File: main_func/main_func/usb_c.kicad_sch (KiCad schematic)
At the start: 6 parts, among them J1 USB_C_Receptacle_USB2.0, J2 Conn_01x05_Male

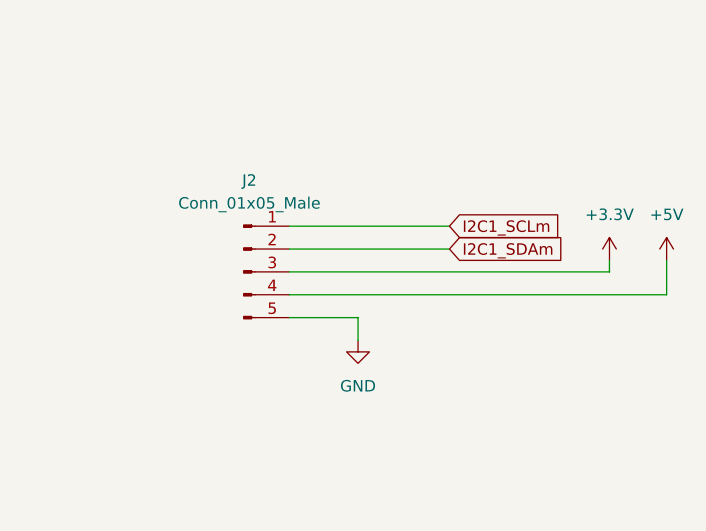
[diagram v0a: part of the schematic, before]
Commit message: main func schematics fixed
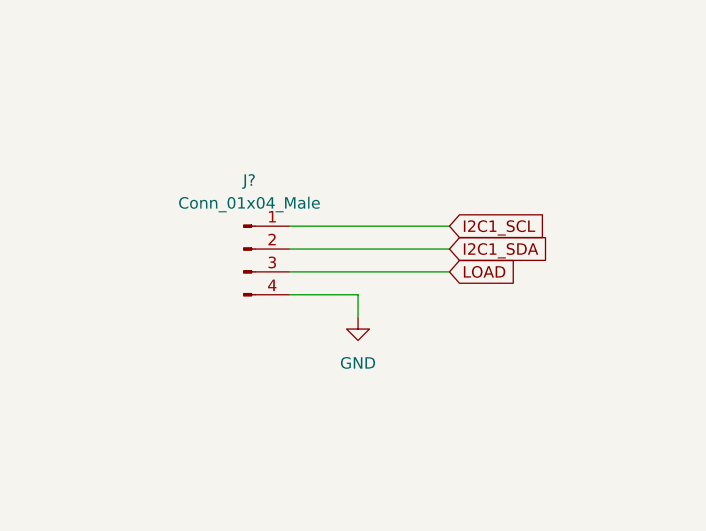
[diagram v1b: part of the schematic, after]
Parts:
- removed J2: Conn_01x05_Male, symbol Connector:Conn_01x05_Male
- added J?: Conn_01x04_Male, symbol Connector:Conn_01x04_Male
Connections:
- net GND: now also J?.4 (Pin_4)
- new net I2C1_SCL: J?.1 (Pin_1)
- new net I2C1_SDA: J?.2 (Pin_2)
- new net LOAD: J?.3 (Pin_3)
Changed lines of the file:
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@@
-    (stroke (width 0) (type default) (color 0 0 0 0))
-  )
-  (wire (pts (xy 163.83 69.85) (xy 205.74 69.85))
     (stroke (width 0) (type default) (color 0 0 0 0))
   )
@@
     (stroke (width 0) (type default) (color 0 0 0 0))
   )
-  (wire (pts (xy 171.45 72.39) (xy 171.45 74.93))
+  (wire (pts (xy 171.45 69.85) (xy 171.45 72.39))
     (stroke (width 0) (type default) (color 0 0 0 0))
   )
@@
     (stroke (width 0) (type default) (color 0 0 0 0))
   )
-  (wire (pts (xy 163.83 72.39) (xy 171.45 72.39))
+  (wire (pts (xy 163.83 69.85) (xy 171.45 69.85))
+    (stroke (width 0) (type default) (color 0 0 0 0))
+  )
+  (wire (pts (xy 163.83 67.31) (xy 181.61 67.31))
     (stroke (width 0) (type default) (color 0 0 0 0))
   )
@@
     (stroke (width 0) (type default) (color 0 0 0 0))
   )
-  (wire (pts (xy 205.74 69.85) (xy 205.74 66.04))
-    (stroke (width 0) (type default) (color 0 0 0 0))
-  )
-  (wire (pts (xy 163.83 67.31) (xy 199.39 67.31))
-    (stroke (width 0) (type default) (color 0 0 0 0))
-  )
   (wire (pts (xy 68.58 44.45) (xy 81.28 44.45))
     (stroke (width 0) (type default) (color 0 0 0 0))
@@
     (stroke (width 0) (type default) (color 0 0 0 0))
   )
-  (wire (pts (xy 199.39 67.31) (xy 199.39 66.04))
-    (stroke (width 0) (type default) (color 0 0 0 0))
-  )
   (wire (pts (xy 68.58 62.23) (xy 73.66 62.23))
     (stroke (width 0) (type default) (color 0 0 0 0))
@@
     )
   )
-  (global_label "I2C1_SDAm" (shape input) (at 181.61 64.77 0) (fields_autoplaced)
-    (effects (font (size 1.27 1.27)) (justify left))
-    (property "Intersheet References" "${INTERSHEET_REFS}" (id 0) (at 194.546 64.6906 0)
+  (global_label "I2C1_SDA" (shape input) (at 181.61 64.77 0) (fields_autoplaced)
+    (effects (font (size 1.27 1.27)) (justify left))
+    (property "Intersheet References" "${INTERSHEET_REFS}" (id 0) (at 192.8526 64.6906 0)
       (effects (font (size 1.27 1.27)) (justify left) hide)
     )
@@
     )
   )
-  (global_label "I2C1_SCLm" (shape input) (at 181.61 62.23 0) (fields_autoplaced)
-    (effects (font (size 1.27 1.27)) (justify left))
-    (property "Intersheet References" "${INTERSHEET_REFS}" (id 0) (at 194.4855 62.1506 0)
-      (effects (font (size 1.27 1.27)) (justify left) hide)
-    )
-  )
-  (symbol (lib_id "power:+5V") (at 205.74 66.04 0) (unit 1)
-    (in_bom yes) (on_board yes) (fields_autoplaced)
-    (property "Reference" "#PWR032" (id 0) (at 205.74 69.85 0)
-      (effects (font (size 1.27 1.27)) hide)
-    )
-    (property "Value" "+5V" (id 1) (at 205.74 60.96 0))
-    (property "Footprint" "" (id 2) (at 205.74 66.04 0)
-      (effects (font (size 1.27 1.27)) hide)
-    )
-    (property "Datasheet" "" (id 3) (at 205.74 66.04 0)
-      (effects (font (size 1.27 1.27)) hide)
-    )
-    (pin "1")
+  (global_label "I2C1_SCL" (shape input) (at 181.61 62.23 0) (fields_autoplaced)
+    (effects (font (size 1.27 1.27)) (justify left))
+    (property "Intersheet References" "${INTERSHEET_REFS}" (id 0) (at 192.7921 62.1506 0)
+      (effects (font (size 1.27 1.27)) (justify left) hide)
+    )
+  )
+  (global_label "LOAD" (shape input) (at 181.61 67.31 0) (fields_autoplaced)
+    (effects (font (size 1.27 1.27)) (justify left))
+    (property "Intersheet References" "${INTERSHEET_REFS}" (id 0) (at 188.7402 67.2306 0)
+      (effects (font (size 1.27 1.27)) (justify left) hide)
+    )
   )
   (symbol (lib_id "Device:R") (at 110.49 58.42 0) (unit 1)
@@
     (pin "2")
   )
-  (symbol (lib_id "power:+3.3V") (at 199.39 66.04 0) (unit 1)
-    (in_bom yes) (on_board yes) (fields_autoplaced)
-    (property "Reference" "#PWR031" (id 0) (at 199.39 69.85 0)
-      (effects (font (size 1.27 1.27)) hide)
-    )
-    (property "Value" "+3.3V" (id 1) (at 199.39 60.96 0))
-    (property "Footprint" "" (id 2) (at 199.39 66.04 0)
-      (effects (font (size 1.27 1.27)) hide)
-    )
-    (property "Datasheet" "" (id 3) (at 199.39 66.04 0)
-      (effects (font (size 1.27 1.27)) hide)
-    )
-    (pin "1")
-  )
   (symbol (lib_id "Device:R") (at 99.06 58.42 0) (unit 1)
     (in_bom yes) (on_board yes) (fields_autoplaced)
@@
     (pin "1")
     (pin "2")
-  )
-  (symbol (lib_id "Connector:Conn_01x05_Male") (at 158.75 67.31 0) (unit 1)
-    (in_bom yes) (on_board yes) (fields_autoplaced)
-    (property "Reference" "J2" (id 0) (at 159.385 57.15 0))
-    (property "Value" "Conn_01x05_Male" (id 1) (at 159.385 59.69 0))
-    (property "Footprint" "" (id 2) (at 158.75 67.31 0)
-      (effects (font (size 1.27 1.27)) hide)
-    )
-    (property "Datasheet" "~" (id 3) (at 158.75 67.31 0)
-      (effects (font (size 1.27 1.27)) hide)
-    )
-    (pin "1")
-    (pin "2")
-    (pin "3")
-    (pin "4")
-    (pin "5")
   )
   (symbol (lib_id "Connector:USB_C_Receptacle_USB2.0") (at 53.34 59.69 0) (unit 1)
@@
     (pin "S1")
   )
+  (symbol (lib_id "Connector:Conn_01x04_Male") (at 158.75 64.77 0) (unit 1)
+    (in_bom yes) (on_board yes) (fields_autoplaced)
+    (property "Reference" "J?" (id 0) (at 159.385 57.15 0))
+    (property "Value" "Conn_01x04_Male" (id 1) (at 159.385 59.69 0))
+    (property "Footprint" "" (id 2) (at 158.75 64.77 0)
+      (effects (font (size 1.27 1.27)) hide)
+    )
+    (property "Datasheet" "~" (id 3) (at 158.75 64.77 0)
+      (effects (font (size 1.27 1.27)) hide)
+    )
+    (pin "1")
+    (pin "2")
+    (pin "3")
+    (pin "4")
+  )
   (symbol (lib_id "Device:Polyfuse") (at 85.09 44.45 90) (unit 1)
     (in_bom yes) (on_board yes) (fields_autoplaced)
@@
     (pin "1")
   )
-  (symbol (lib_id "power:GND") (at 171.45 74.93 0) (unit 1)
-    (in_bom yes) (on_board yes) (fields_autoplaced)
-    (property "Reference" "#PWR030" (id 0) (at 171.45 81.28 0)
-      (effects (font (size 1.27 1.27)) hide)
-    )
-    (property "Value" "GND" (id 1) (at 171.45 80.01 0))
-    (property "Footprint" "" (id 2) (at 171.45 74.93 0)
-      (effects (font (size 1.27 1.27)) hide)
-    )
-    (property "Datasheet" "" (id 3) (at 171.45 74.93 0)
-      (effects (font (size 1.27 1.27)) hide)
-    )
+  (symbol (lib_id "power:GND") (at 171.45 72.39 0) (unit 1)
+    (in_bom yes) (on_board yes) (fields_autoplaced)
+    (property "Reference" "#PWR030" (id 0) (at 171.45 78.74 0)
+      (effects (font (size 1.27 1.27)) hide)
+    )
+    (property "Value" "GND" (id 1) (at 171.45 77.47 0))
+    (property "Footprint" "" (id 2) (at 171.45 72.39 0)
+      (effects (font (size 1.27 1.27)) hide)
+    )
+    (property "Datasheet" "" (id 3) (at 171.45 72.39 0)
+      (effects (font (size 1.27 1.27)) hide)
+    )

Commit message: fixing keyboard and pot project schematics
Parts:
- gave numbers to parts that had none: 1
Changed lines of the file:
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@@
   (symbol (lib_id "Connector:Conn_01x04_Male") (at 158.75 64.77 0) (unit 1)
     (in_bom yes) (on_board yes) (fields_autoplaced)
-    (property "Reference" "J?" (id 0) (at 159.385 57.15 0))
+    (property "Reference" "J2" (id 0) (at 159.385 57.15 0))
     (property "Value" "Conn_01x04_Male" (id 1) (at 159.385 59.69 0))
     (property "Footprint" "" (id 2) (at 158.75 64.77 0)

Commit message: main_func pcb done
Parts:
- J2: footprint (none) -> Connector_PinHeader_2.54mm:PinHeader_1x04_P2.54mm_Horizontal
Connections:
- net I2C1_SCL: now also J2.2 (Pin_2); no longer J2.1 (Pin_1)
- net I2C1_SDA: now also J2.1 (Pin_1); no longer J2.2 (Pin_2)
- net USB_D+ renamed USB_DP1m
- net USB_D- renamed USB_DM1m
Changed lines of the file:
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@@
     (stroke (width 0) (type default) (color 0 0 0 0))
-  )
-  (global_label "USB_D+" (shape input) (at 81.28 62.23 0) (fields_autoplaced)
-    (effects (font (size 1.27 1.27)) (justify left))
-    (property "Intersheet References" "${INTERSHEET_REFS}" (id 0) (at 91.3131 62.1506 0)
-      (effects (font (size 1.27 1.27)) (justify left) hide)
-    )
   )
   (global_label "USB_Input_supply" (shape input) (at 100.33 44.45 0) (fields_autoplaced)
@@
     )
   )
-  (global_label "I2C1_SDA" (shape input) (at 181.61 64.77 0) (fields_autoplaced)
+  (global_label "I2C1_SCL" (shape input) (at 181.61 64.77 0) (fields_autoplaced)
     (effects (font (size 1.27 1.27)) (justify left))
-    (property "Intersheet References" "${INTERSHEET_REFS}" (id 0) (at 192.8526 64.6906 0)
+    (property "Intersheet References" "${INTERSHEET_REFS}" (id 0) (at 192.7921 64.6906 0)
       (effects (font (size 1.27 1.27)) (justify left) hide)
     )
   )
-  (global_label "USB_D-" (shape input) (at 81.28 57.15 0) (fields_autoplaced)
+  (global_label "USB_DM1m" (shape input) (at 81.28 57.15 0) (fields_autoplaced)
     (effects (font (size 1.27 1.27)) (justify left))
-    (property "Intersheet References" "${INTERSHEET_REFS}" (id 0) (at 91.3131 57.0706 0)
+    (property "Intersheet References" "${INTERSHEET_REFS}" (id 0) (at 94.095 57.0706 0)
       (effects (font (size 1.27 1.27)) (justify left) hide)
     )
   )
-  (global_label "I2C1_SCL" (shape input) (at 181.61 62.23 0) (fields_autoplaced)
+  (global_label "I2C1_SDA" (shape input) (at 181.61 62.23 0) (fields_autoplaced)
     (effects (font (size 1.27 1.27)) (justify left))
-    (property "Intersheet References" "${INTERSHEET_REFS}" (id 0) (at 192.7921 62.1506 0)
+    (property "Intersheet References" "${INTERSHEET_REFS}" (id 0) (at 192.8526 62.1506 0)
       (effects (font (size 1.27 1.27)) (justify left) hide)
     )
@@
     (effects (font (size 1.27 1.27)) (justify left))
     (property "Intersheet References" "${INTERSHEET_REFS}" (id 0) (at 188.7402 67.2306 0)
+      (effects (font (size 1.27 1.27)) (justify left) hide)
+    )
+  )
+  (global_label "USB_DP1m" (shape input) (at 81.28 62.23 0) (fields_autoplaced)
+    (effects (font (size 1.27 1.27)) (justify left))
+    (property "Intersheet References" "${INTERSHEET_REFS}" (id 0) (at 93.9136 62.1506 0)
       (effects (font (size 1.27 1.27)) (justify left) hide)
     )
@@
     (property "Reference" "J2" (id 0) (at 159.385 57.15 0))
     (property "Value" "Conn_01x04_Male" (id 1) (at 159.385 59.69 0))
-    (property "Footprint" "" (id 2) (at 158.75 64.77 0)
+    (property "Footprint" "Connector_PinHeader_2.54mm:PinHeader_1x04_P2.54mm_Horizontal" (id 2) (at 158.75 64.77 0)
       (effects (font (size 1.27 1.27)) hide)
     )

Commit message: pcb design fixing
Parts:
- removed J2: Conn_01x04_Male, Connector_PinHeader_2.54mm:PinHeader_1x04_P2.54mm_Horizontal, symbol Connector:Conn_01x04_Male
- added J2, J3: Conn_01x10_Male, Connector_IDC:IDC-Header_2x05_P2.54mm_Horizontal, symbol Connector:Conn_01x10_Male
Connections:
- net GND: now also J2.10 (Pin_10), J2.2 (Pin_2), J2.4 (Pin_4), J2.6 (Pin_6), J2.8 (Pin_8), J2.9 (Pin_9), J3.10 (Pin_10), J3.2 (Pin_2), J3.4 (Pin_4), J3.6 (Pin_6), J3.8 (Pin_8), J3.9 (Pin_9)
- net I2C1_SCL: now also J2.7 (Pin_7), J3.7 (Pin_7)
- net I2C1_SDA: now also J2.5 (Pin_5), J3.5 (Pin_5)
- net LOAD: now also J2.1 (Pin_1), J2.3 (Pin_3), J3.1 (Pin_1), J3.3 (Pin_3)

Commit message: gerber files generated
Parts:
- added H1, H2, H3, H4, H5: MountingHole, MountingHole:MountingHole_3.2mm_M3_Pad_Via, symbol Mechanical:MountingHole
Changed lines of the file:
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@@
     (pin "1")
+  )
+  (symbol (lib_id "Mechanical:MountingHole") (at 231.14 35.56 0) (unit 1)
+    (in_bom yes) (on_board yes) (fields_autoplaced)
+    (property "Reference" "H4" (id 0) (at 233.68 34.2899 0)
+      (effects (font (size 1.27 1.27)) (justify left))
+    )
+    (property "Value" "MountingHole" (id 1) (at 233.68 36.8299 0)
+      (effects (font (size 1.27 1.27)) (justify left))
+    )
+    (property "Footprint" "MountingHole:MountingHole_3.2mm_M3_Pad_Via" (id 2) (at 231.14 35.56 0)
+      (effects (font (size 1.27 1.27)) hide)
+    )
+    (property "Datasheet" "~" (id 3) (at 231.14 35.56 0)
+      (effects (font (size 1.27 1.27)) hide)
+    )
   )
   (symbol (lib_id "Device:R") (at 99.06 58.42 0) (unit 1)
@@
     (pin "1")
     (pin "2")
+  )
+  (symbol (lib_id "Mechanical:MountingHole") (at 187.96 35.56 0) (unit 1)
+    (in_bom yes) (on_board yes) (fields_autoplaced)
+    (property "Reference" "H2" (id 0) (at 190.5 34.2899 0)
+      (effects (font (size 1.27 1.27)) (justify left))
+    )
+    (property "Value" "MountingHole" (id 1) (at 190.5 36.8299 0)
+      (effects (font (size 1.27 1.27)) (justify left))
+    )
+    (property "Footprint" "MountingHole:MountingHole_3.2mm_M3_Pad_Via" (id 2) (at 187.96 35.56 0)
+      (effects (font (size 1.27 1.27)) hide)
+    )
+    (property "Datasheet" "~" (id 3) (at 187.96 35.56 0)
+      (effects (font (size 1.27 1.27)) hide)
+    )
   )
   (symbol (lib_id "Connector:USB_C_Receptacle_USB2.0") (at 53.34 59.69 0) (unit 1)
@@
     (pin "S1")
   )
+  (symbol (lib_id "Mechanical:MountingHole") (at 165.1 35.56 0) (unit 1)
+    (in_bom yes) (on_board yes) (fields_autoplaced)
+    (property "Reference" "H1" (id 0) (at 167.64 34.2899 0)
+      (effects (font (size 1.27 1.27)) (justify left))
+    )
+    (property "Value" "MountingHole" (id 1) (at 167.64 36.8299 0)
+      (effects (font (size 1.27 1.27)) (justify left))
+    )
+    (property "Footprint" "MountingHole:MountingHole_3.2mm_M3_Pad_Via" (id 2) (at 165.1 35.56 0)
+      (effects (font (size 1.27 1.27)) hide)
+    )
+    (property "Datasheet" "~" (id 3) (at 165.1 35.56 0)
+      (effects (font (size 1.27 1.27)) hide)
+    )
+  )
   (symbol (lib_id "power:GND") (at 199.39 118.11 0) (unit 1)
     (in_bom yes) (on_board yes) (fields_autoplaced)
@@
     (pin "9")
   )
+  (symbol (lib_id "Mechanical:MountingHole") (at 251.46 35.56 0) (unit 1)
+    (in_bom yes) (on_board yes) (fields_autoplaced)
+    (property "Reference" "H5" (id 0) (at 254 34.2899 0)
+      (effects (font (size 1.27 1.27)) (justify left))
+    )
+    (property "Value" "MountingHole" (id 1) (at 254 36.8299 0)
+      (effects (font (size 1.27 1.27)) (justify left))
+    )
+    (property "Footprint" "MountingHole:MountingHole_3.2mm_M3_Pad_Via" (id 2) (at 251.46 35.56 0)
+      (effects (font (size 1.27 1.27)) hide)
+    )
+    (property "Datasheet" "~" (id 3) (at 251.46 35.56 0)
+      (effects (font (size 1.27 1.27)) hide)
+    )
+  )
   (symbol (lib_id "power:GND") (at 99.06 62.23 0) (unit 1)
     (in_bom yes) (on_board yes) (fields_autoplaced)
@@
     (pin "1")
   )
+  (symbol (lib_id "Mechanical:MountingHole") (at 209.55 35.56 0) (unit 1)
+    (in_bom yes) (on_board yes) (fields_autoplaced)
+    (property "Reference" "H3" (id 0) (at 212.09 34.2899 0)
+      (effects (font (size 1.27 1.27)) (justify left))
+    )
+    (property "Value" "MountingHole" (id 1) (at 212.09 36.8299 0)
+      (effects (font (size 1.27 1.27)) (justify left))
+    )
+    (property "Footprint" "MountingHole:MountingHole_3.2mm_M3_Pad_Via" (id 2) (at 209.55 35.56 0)
+      (effects (font (size 1.27 1.27)) hide)
+    )
+    (property "Datasheet" "~" (id 3) (at 209.55 35.56 0)
+      (effects (font (size 1.27 1.27)) hide)
+    )
+  )
 )
